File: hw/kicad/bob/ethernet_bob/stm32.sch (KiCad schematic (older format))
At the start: 2 parts, among them P1 USB_OTG, U2 STM32F407VETx

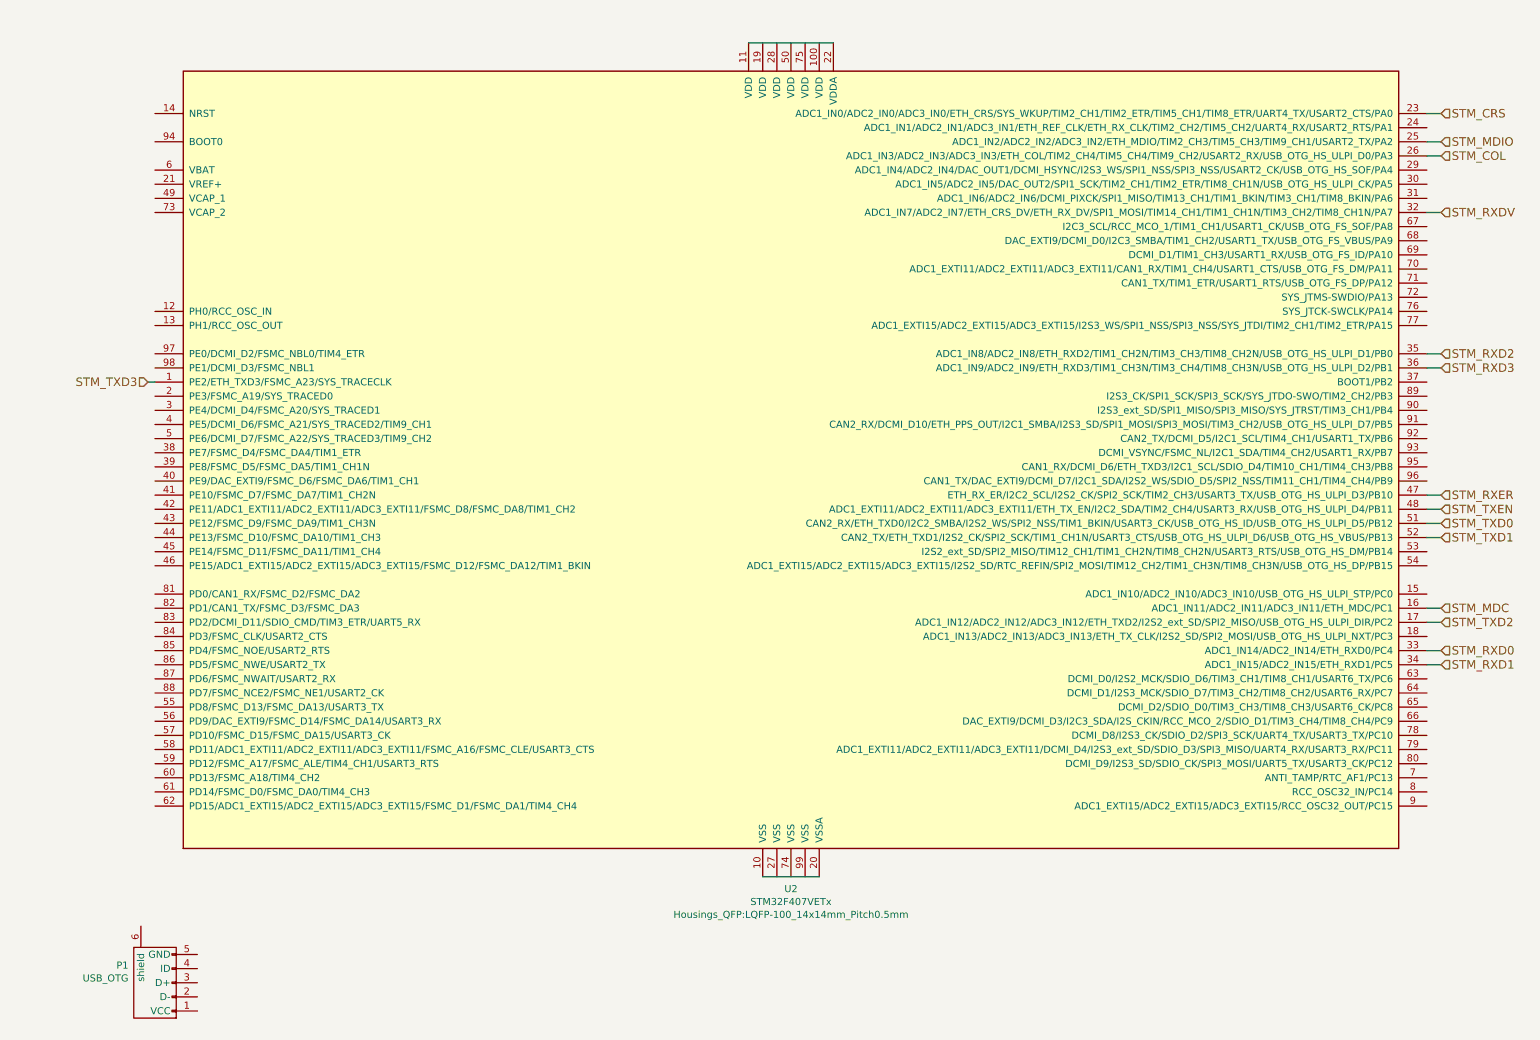
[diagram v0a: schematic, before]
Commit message: Changed over to RMII, I think...
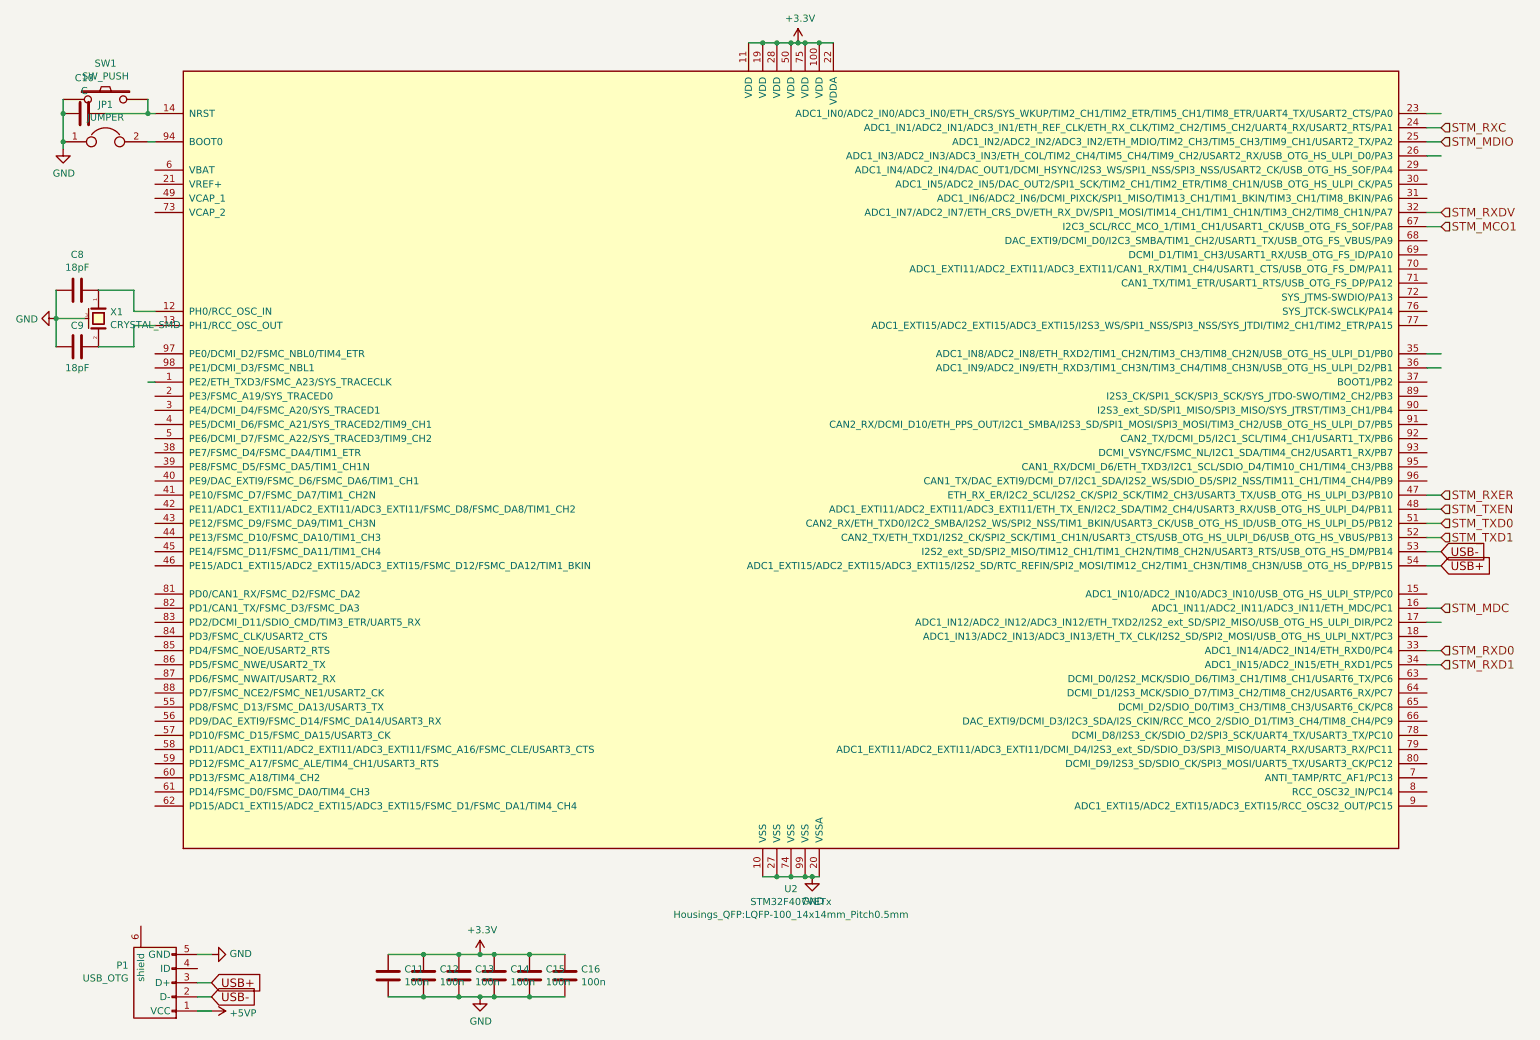
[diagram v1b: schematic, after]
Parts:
- added C10: C, Capacitors_SMD:C_0603, symbol C
- added C11, C12, C13, C14, C15, C16: 100n, Capacitors_SMD:C_0603, symbol C
- added C8, C9: 18pF, Capacitors_SMD:C_0603, symbol C
- added JP1: JUMPER, Capacitors_SMD:C_0603, symbol JUMPER
- added SW1: SW_PUSH, symbol SW_PUSH
- added X1: CRYSTAL_SMD, Crystals:Crystal_SMD_0603_4Pads, symbol CRYSTAL_SMD
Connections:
- net labels added: +3.3V, +5VP, GND, STM_MCO1, STM_RXC, USB+, USB-
- net labels removed: STM_COL, STM_CRS, STM_RXD2, STM_RXD3, STM_TXD2, STM_TXD3
- wire segments 17 -> 39

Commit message: Chang RJ45 footprint to represent the right one. Add pin headers. Add reset button. Add power supply.
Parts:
- added P2, P3, P4: CONN_02X16, Pin_Headers:Pin_Header_Straight_2x16, symbol CONN_02X16
- SW1: footprint (none) -> Buttons_Switches_SMD:SW_SPST_EVQQ2
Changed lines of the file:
@@
 F 0 "SW1" H 950 1355 50  0000 C CNN
 F 1 "SW_PUSH" H 950 1264 50  0000 C CNN
-F 2 "" H 950 1100 50  0001 C CNN
+F 2 "Buttons_Switches_SMD:SW_SPST_EVQQ2" H 950 1100 50  0001 C CNN
 F 3 "" H 950 1100 50  0000 C CNN
 	1    950  1100
@@
 Text HLabel 10400 3900 2    60   Input ~ 0
 STM_RXER
+$Comp
+L CONN_02X16 P2
+U 1 1 57C44F8D
+P 12850 3700
+F 0 "P2" H 12850 4665 50  0000 C CNN
+F 1 "CONN_02X16" H 12850 4574 50  0000 C CNN
+F 2 "Pin_Headers:Pin_Header_Straight_2x16" H 12850 2600 50  0001 C CNN
+F 3 "" H 12850 2600 50  0000 C CNN
+	1    12850 3700
+	1    0    0    -1
+$EndComp
+$Comp
+L CONN_02X16 P3
+U 1 1 57C45008
+P 12850 5550
+F 0 "P3" H 12850 6515 50  0000 C CNN
+F 1 "CONN_02X16" H 12850 6424 50  0000 C CNN
+F 2 "Pin_Headers:Pin_Header_Straight_2x16" H 12850 4450 50  0001 C CNN
+F 3 "" H 12850 4450 50  0000 C CNN
+	1    12850 5550
+	1    0    0    -1
+$EndComp
+$Comp
+L CONN_02X16 P4
+U 1 1 57C45096
+P 12850 7450
+F 0 "P4" H 12850 8415 50  0000 C CNN
+F 1 "CONN_02X16" H 12850 8324 50  0000 C CNN
+F 2 "Pin_Headers:Pin_Header_Straight_2x16" H 12850 6350 50  0001 C CNN
+F 3 "" H 12850 6350 50  0000 C CNN
+	1    12850 7450
+	1    0    0    -1
+$EndComp
 $EndSCHEMATC

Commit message: changed over to disco header
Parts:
- removed P2, P3, P4: CONN_02X16, Pin_Headers:Pin_Header_Straight_2x16, symbol CONN_02X16
- added P2, P3: CONN_02X25, Pin_Headers:Pin_Header_Straight_2x25, symbol CONN_02X25
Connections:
- net labels added: +3V3, BOOT0, NRST, PA0, PA1, PA10, PA13, PA14, PA15, PA2, PA3, PA4, PA5, PA6, PA7, PA8, PA9, PB0, PB1, PB10, PB11, PB12, PB13, PB14, PB15, PB2, PB3, PB4, PB5, PB6, PB7, PB8, PB9, PC0, PC1, PC10, PC11, PC12, PC13, PC14, PC15, PC2, PC3, PC4, PC5, PC6, PC7, PC8, PC9, PD0, PD1, PD10, PD11, PD12, PD13, PD14, PD15, PD2, PD3, PD4, PD5, PD6, PD7, PD8, PD9, PE0, PE1, PE10, PE11, PE12, PE13, PE14, PE15, PE2, PE3, PE4, PE5, PE6, PE7, PE8, PE9, PH0, PH1
- wire segments 39 -> 196

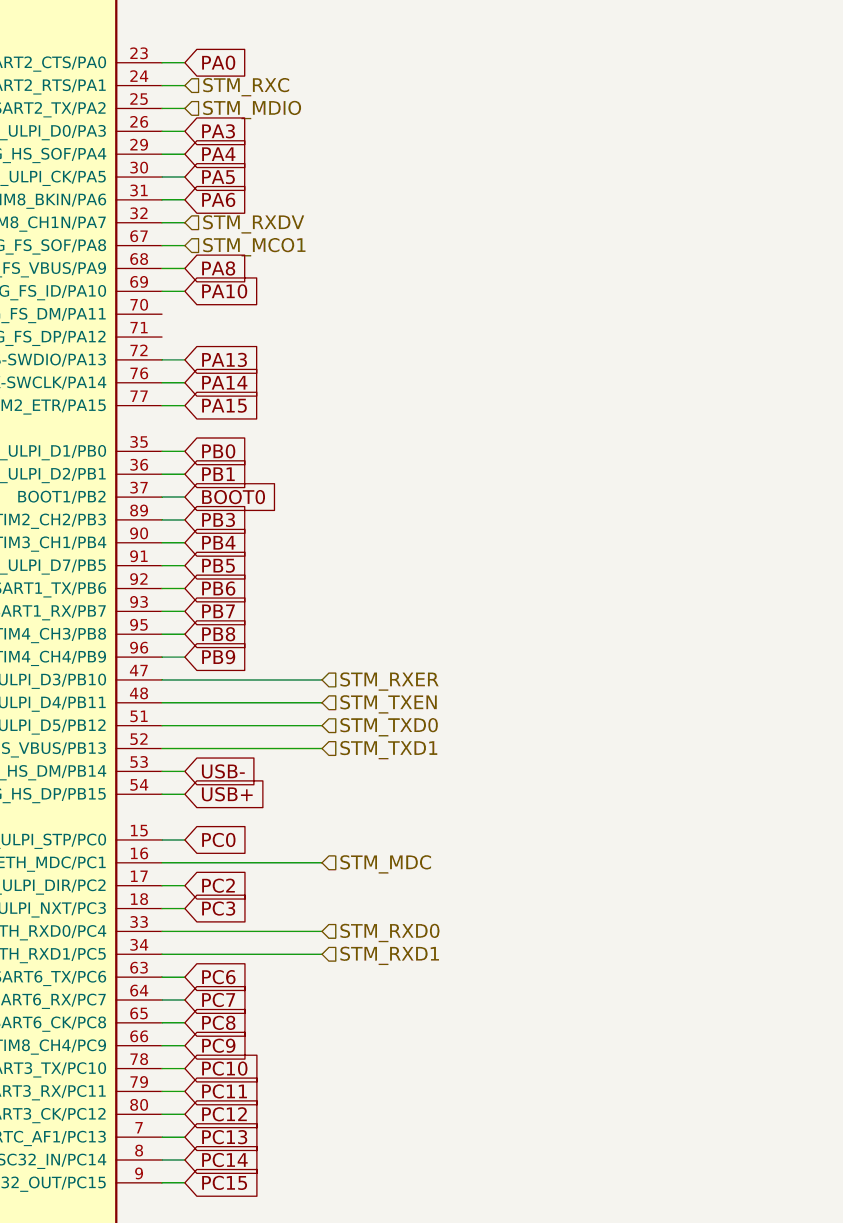
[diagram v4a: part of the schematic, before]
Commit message: add selectable MCO
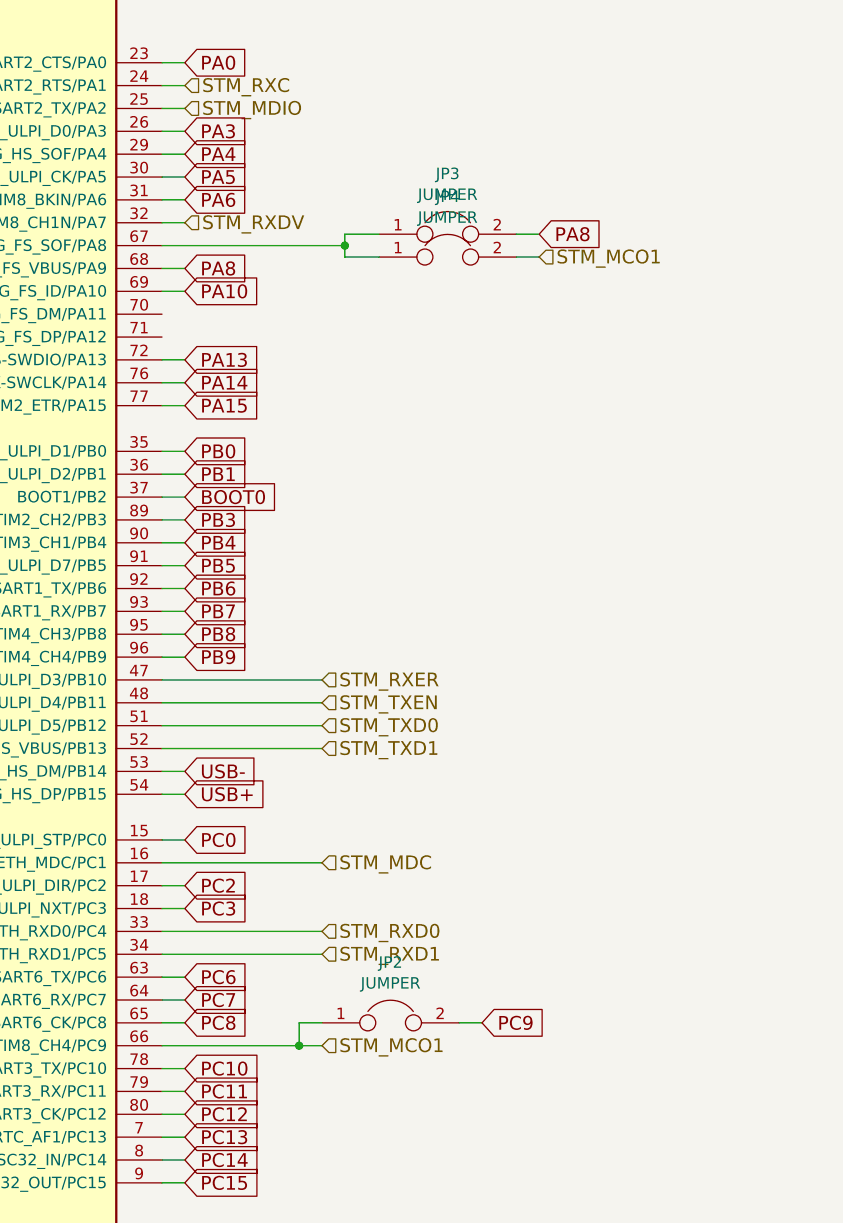
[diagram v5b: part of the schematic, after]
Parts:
- added JP2, JP3, JP4: JUMPER, Capacitors_SMD:C_0603, symbol JUMPER
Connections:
- net PA8: now also JP3.2
- net PC9: now also JP2.2; no longer U2.66 (DAC_EXTI9/DCMI_D3/I2C3_SDA/I2S_CKIN/RCC_MCO_2/SDIO_D1/TIM3_CH4/TIM8_CH4/PC9)
- net STM_MCO1: now also U2.66 (DAC_EXTI9/DCMI_D3/I2C3_SDA/I2S_CKIN/RCC_MCO_2/SDIO_D1/TIM3_CH4/TIM8_CH4/PC9), JP2.1, JP4.2; no longer U2.67 (I2C3_SCL/RCC_MCO_1/TIM1_CH1/USART1_CK/USB_OTG_FS_SOF/PA8)
- new net: JP3.1, JP4.1, U2.67 (I2C3_SCL/RCC_MCO_1/TIM1_CH1/USART1_CK/USB_OTG_FS_SOF/PA8)
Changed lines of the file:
@@
 $Descr A3 16535 11693
 encoding utf-8
-Sheet 2 4
+Sheet 2 3
 Title "STM32 Ethernet BOB"
 Date ""
@@
 	0    1    1    0
 $EndComp
-Text HLabel 10400 2000 2    60   Input ~ 0
+Text HLabel 11950 2050 2    60   Input ~ 0
 STM_MCO1
 $Comp
@@
 	1600 7550 1700 7550
 Wire Wire Line
-	10300 2000 10400 2000
+	10300 2000 11100 2000
 Wire Wire Line
 	2950 7150 4200 7150
@@
 Text GLabel 10400 5400 2    60   Input ~ 0
 PC8
-Text GLabel 10400 5500 2    60   Input ~ 0
-PC9
 Text GLabel 10400 5300 2    60   Input ~ 0
 PC7
@@
 	10300 5600 10400 5600
 Wire Wire Line
-	10300 5500 10400 5500
+	10300 5500 11000 5500
 Wire Wire Line
 	10300 5400 10400 5400
@@
 Wire Wire Line
 	10300 3100 10400 3100
+Text HLabel 11000 5500 2    60   Input ~ 0
+STM_MCO1
+Text GLabel 11700 5400 2    60   Input ~ 0
+PC9
+Wire Wire Line
+	10900 5500 10900 5400
+Wire Wire Line
+	10900 5400 11000 5400
+Connection ~ 10900 5500
+$Comp
+L JUMPER JP2
+U 1 1 57ED2072
+P 11300 5400
+F 0 "JP2" H 11300 5664 50  0000 C CNN
+F 1 "JUMPER" H 11300 5573 50  0000 C CNN
+F 2 "Capacitors_SMD:C_0603" H 11300 5400 50  0001 C CNN
+F 3 "" H 11300 5400 50  0000 C CNN
+	1    11300 5400
+	1    0    0    -1
+$EndComp
+Wire Wire Line
+	11600 5400 11700 5400
+Text GLabel 11950 1950 2    60   Input ~ 0
+PA8
+$Comp
+L JUMPER JP3
+U 1 1 57ED3151
+P 11550 1950
+F 0 "JP3" H 11550 2214 50  0000 C CNN
+F 1 "JUMPER" H 11550 2123 50  0000 C CNN
+F 2 "Capacitors_SMD:C_0603" H 11550 1950 50  0001 C CNN
+F 3 "" H 11550 1950 50  0000 C CNN
+	1    11550 1950
+	1    0    0    -1
+$EndComp
+Wire Wire Line
+	11100 1950 11100 2050
+Wire Wire Line
+	11100 1950 11250 1950
+Wire Wire Line
+	11100 2050 11250 2050
+Connection ~ 11100 2000
+Wire Wire Line
+	11850 1950 11950 1950
+$Comp
+L JUMPER JP4
+U 1 1 57ED26BC
+P 11550 2050
+F 0 "JP4" H 11550 2314 50  0000 C CNN
+F 1 "JUMPER" H 11550 2223 50  0000 C CNN
+F 2 "Capacitors_SMD:C_0603" H 11550 2050 50  0001 C CNN
+F 3 "" H 11550 2050 50  0000 C CNN
+	1    11550 2050
+	1    0    0    -1
+$EndComp
+Wire Wire Line
+	11850 2050 11950 2050
 $EndSCHEMATC

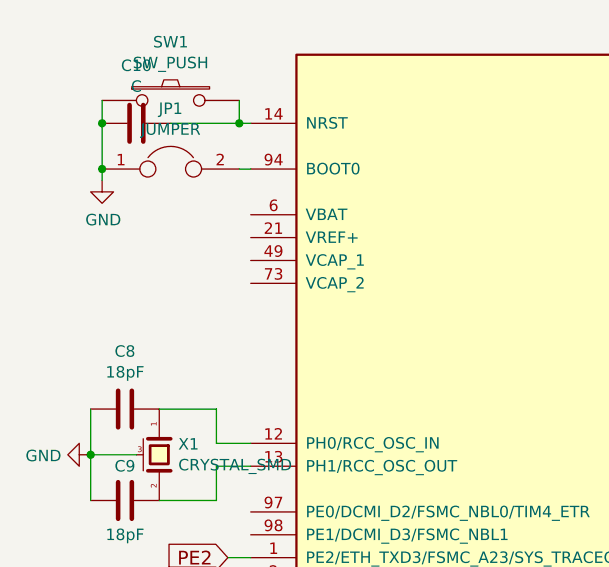
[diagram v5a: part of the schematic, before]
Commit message: add vcap/vref/vbat
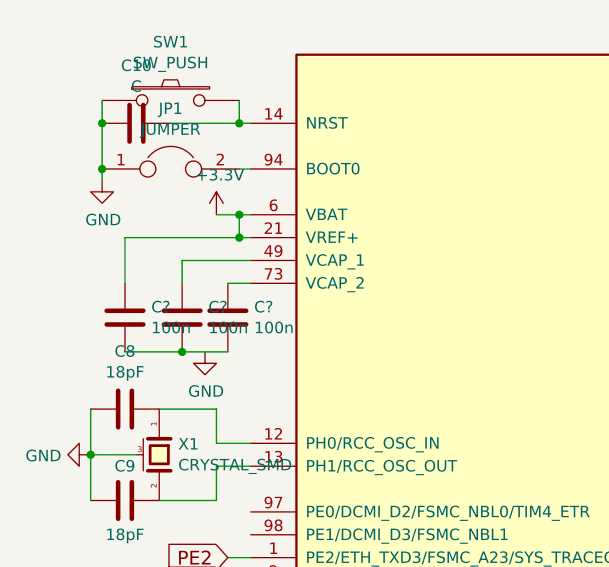
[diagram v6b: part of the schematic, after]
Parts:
- added C? (x3): 100n, Capacitors_SMD:C_0603, symbol C
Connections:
- net +3V3: now also U2.21 (VREF+), U2.6 (VBAT), C?.2
- net at U2.49 (VCAP_1): now also C?.2
- net at U2.73 (VCAP_2): now also C?.2
- new net: C?.1, C?.1, C?.1
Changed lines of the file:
@@
 Wire Wire Line
 	11850 2050 11950 2050
+$Comp
+L C C?
+U 1 1 57ED55B5
+P 1200 2050
+F 0 "C?" H 1085 2004 50  0000 R CNN
+F 1 "100n" H 1085 2095 50  0000 R CNN
+F 2 "Capacitors_SMD:C_0603" H 1238 1900 50  0001 C CNN
+F 3 "" H 1200 2050 50  0000 C CNN
+	1    1200 2050
+	-1   0    0    1
+$EndComp
+$Comp
+L C C?
+U 1 1 57ED57EF
+P 1000 2050
+F 0 "C?" H 885 2004 50  0000 R CNN
+F 1 "100n" H 885 2095 50  0000 R CNN
+F 2 "Capacitors_SMD:C_0603" H 1038 1900 50  0001 C CNN
+F 3 "" H 1000 2050 50  0000 C CNN
+	1    1000 2050
+	-1   0    0    1
+$EndComp
+Wire Wire Line
+	1200 1900 1300 1900
+Wire Wire Line
+	1000 1900 1000 1800
+Wire Wire Line
+	1000 1800 1300 1800
+Wire Wire Line
+	750  2200 1200 2200
+$Comp
+L GND #PWR?
+U 1 1 57ED5C25
+P 1100 2200
+F 0 "#PWR?" H 1100 1950 50  0001 C CNN
+F 1 "GND" H 1105 2027 50  0000 C CNN
+F 2 "" H 1100 2200 50  0000 C CNN
+F 3 "" H 1100 2200 50  0000 C CNN
+	1    1100 2200
+	1    0    0    -1
+$EndComp
+$Comp
+L +3.3V #PWR?
+U 1 1 57ED5D80
+P 1150 1600
+F 0 "#PWR?" H 1150 1450 50  0001 C CNN
+F 1 "+3.3V" H 1165 1773 50  0000 C CNN
+F 2 "" H 1150 1600 50  0000 C CNN
+F 3 "" H 1150 1600 50  0000 C CNN
+	1    1150 1600
+	1    0    0    -1
+$EndComp
+Wire Wire Line
+	1300 1600 1150 1600
+Wire Wire Line
+	1250 1600 1250 1700
+Wire Wire Line
+	750  1700 1300 1700
+Connection ~ 1250 1600
+$Comp
+L C C?
+U 1 1 57ED64E7
+P 750 2050
+F 0 "C?" H 635 2004 50  0000 R CNN
+F 1 "100n" H 635 2095 50  0000 R CNN
+F 2 "Capacitors_SMD:C_0603" H 788 1900 50  0001 C CNN
+F 3 "" H 750 2050 50  0000 C CNN
+	1    750  2050
+	-1   0    0    1
+$EndComp
+Connection ~ 1000 2200
+Wire Wire Line
+	750  1900 750  1700
+Connection ~ 1250 1700
 $EndSCHEMATC
